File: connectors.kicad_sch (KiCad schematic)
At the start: 13 parts, among them J1 Conn_FFC_WE_68715014022, J2 Conn_FAKRA_2FAI-NZSP-PCBB6

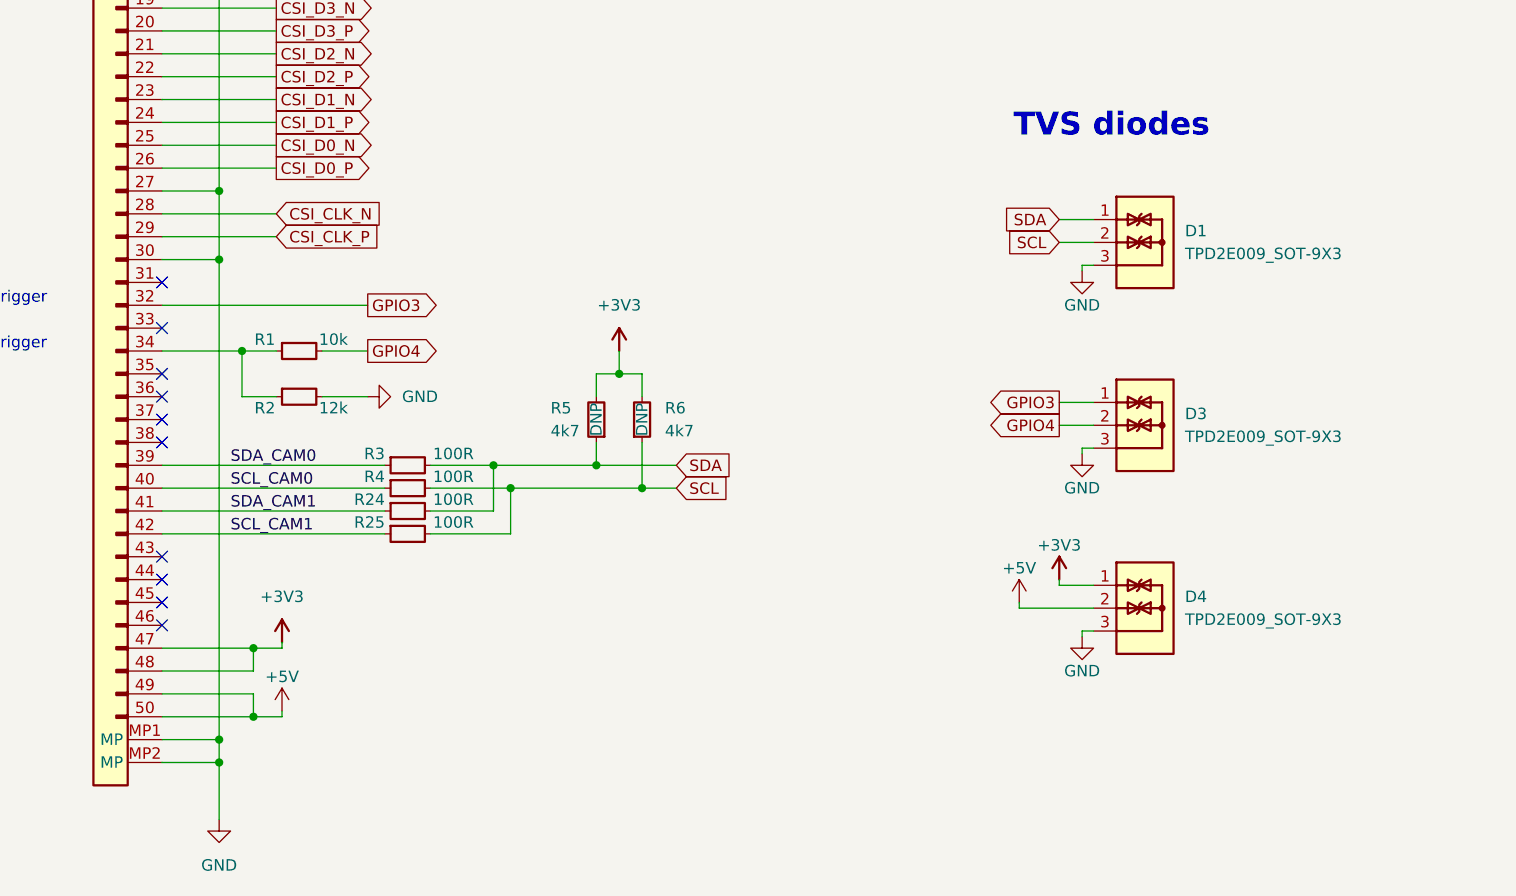
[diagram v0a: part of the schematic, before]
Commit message: Update TVS diodes
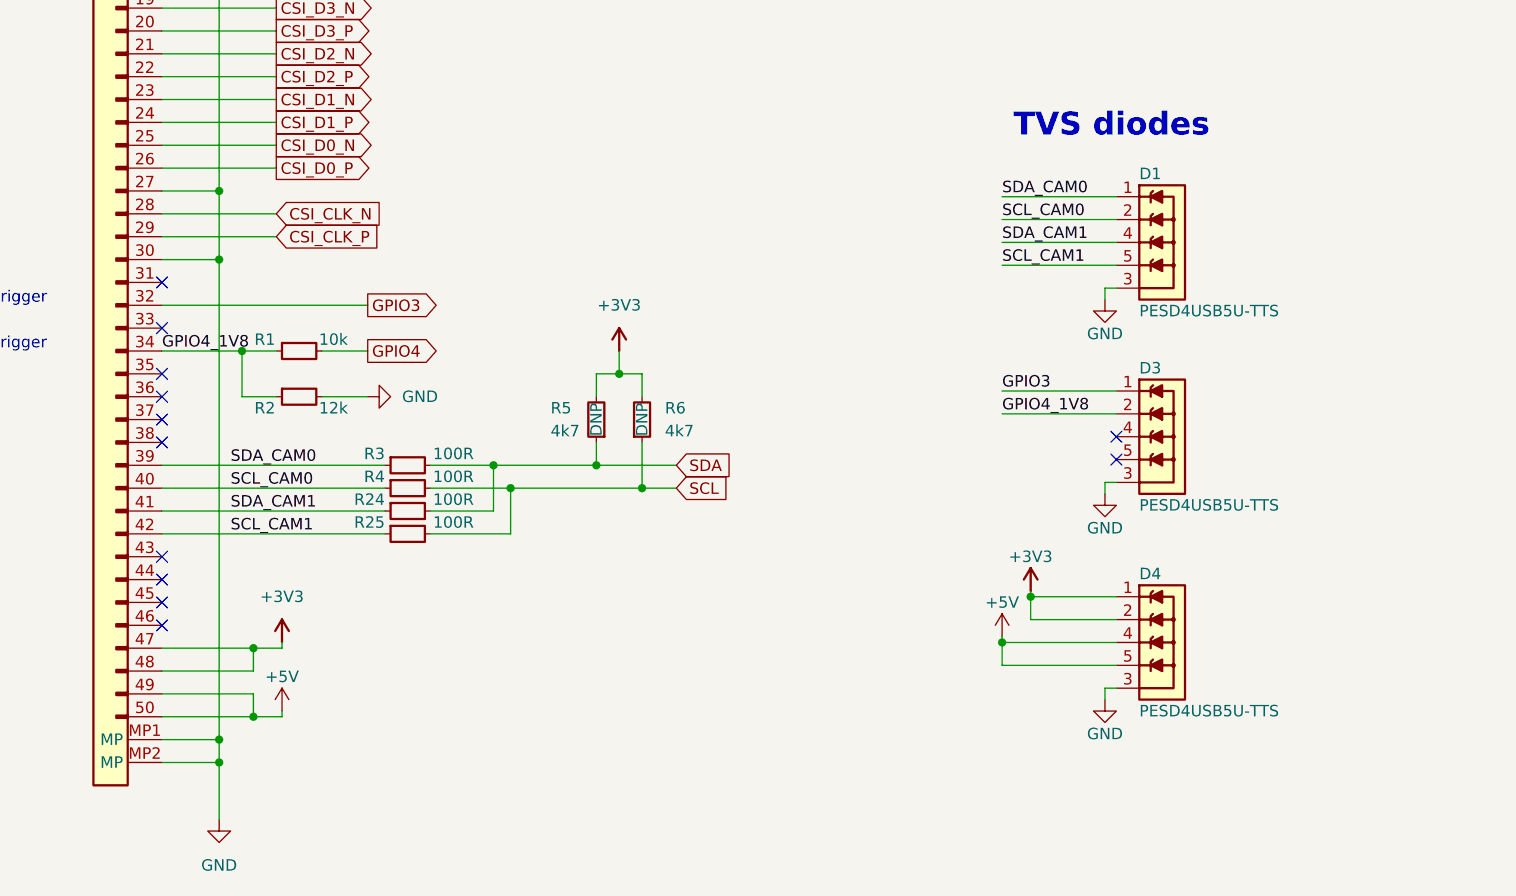
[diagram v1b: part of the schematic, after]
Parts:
- removed D1, D3, D4: TPD2E009_SOT-9X3, antmicro-footprints:SOT-723, symbol antmicroTVSDiodes:TPD2E009_SOT-9X3
- added D1, D3, D4: PESD4USB5U-TTS, antmicro-footprints:DFN-10_2.5x1mm, symbol antmicroTVSDiodes:PESD4USB5U-TTS
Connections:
- net +3V3: now also D4.1, D4.10, D4.2, D4.9
- net +5V: now also D4.4, D4.5, D4.6, D4.7
- net GND: now also D1.3, D1.8, D3.3, D3.8, D4.3, D4.8
- net GPIO3: now also D3.1, D3.10
- net SCL_CAM0: now also D1.2, D1.9
- net SCL_CAM1: now also D1.5, D1.6
- net SDA_CAM0: now also D1.1, D1.10
- net SDA_CAM1: now also D1.4, D1.7
- net GPIO4_1V8: now reaches J1.34, R1.1, R2.1
- net GPIO4_1V8: now also D3.2, D3.9
- new net: D3.4, D3.7
- new net: D3.5, D3.6
- no-connect marks 24 -> 26

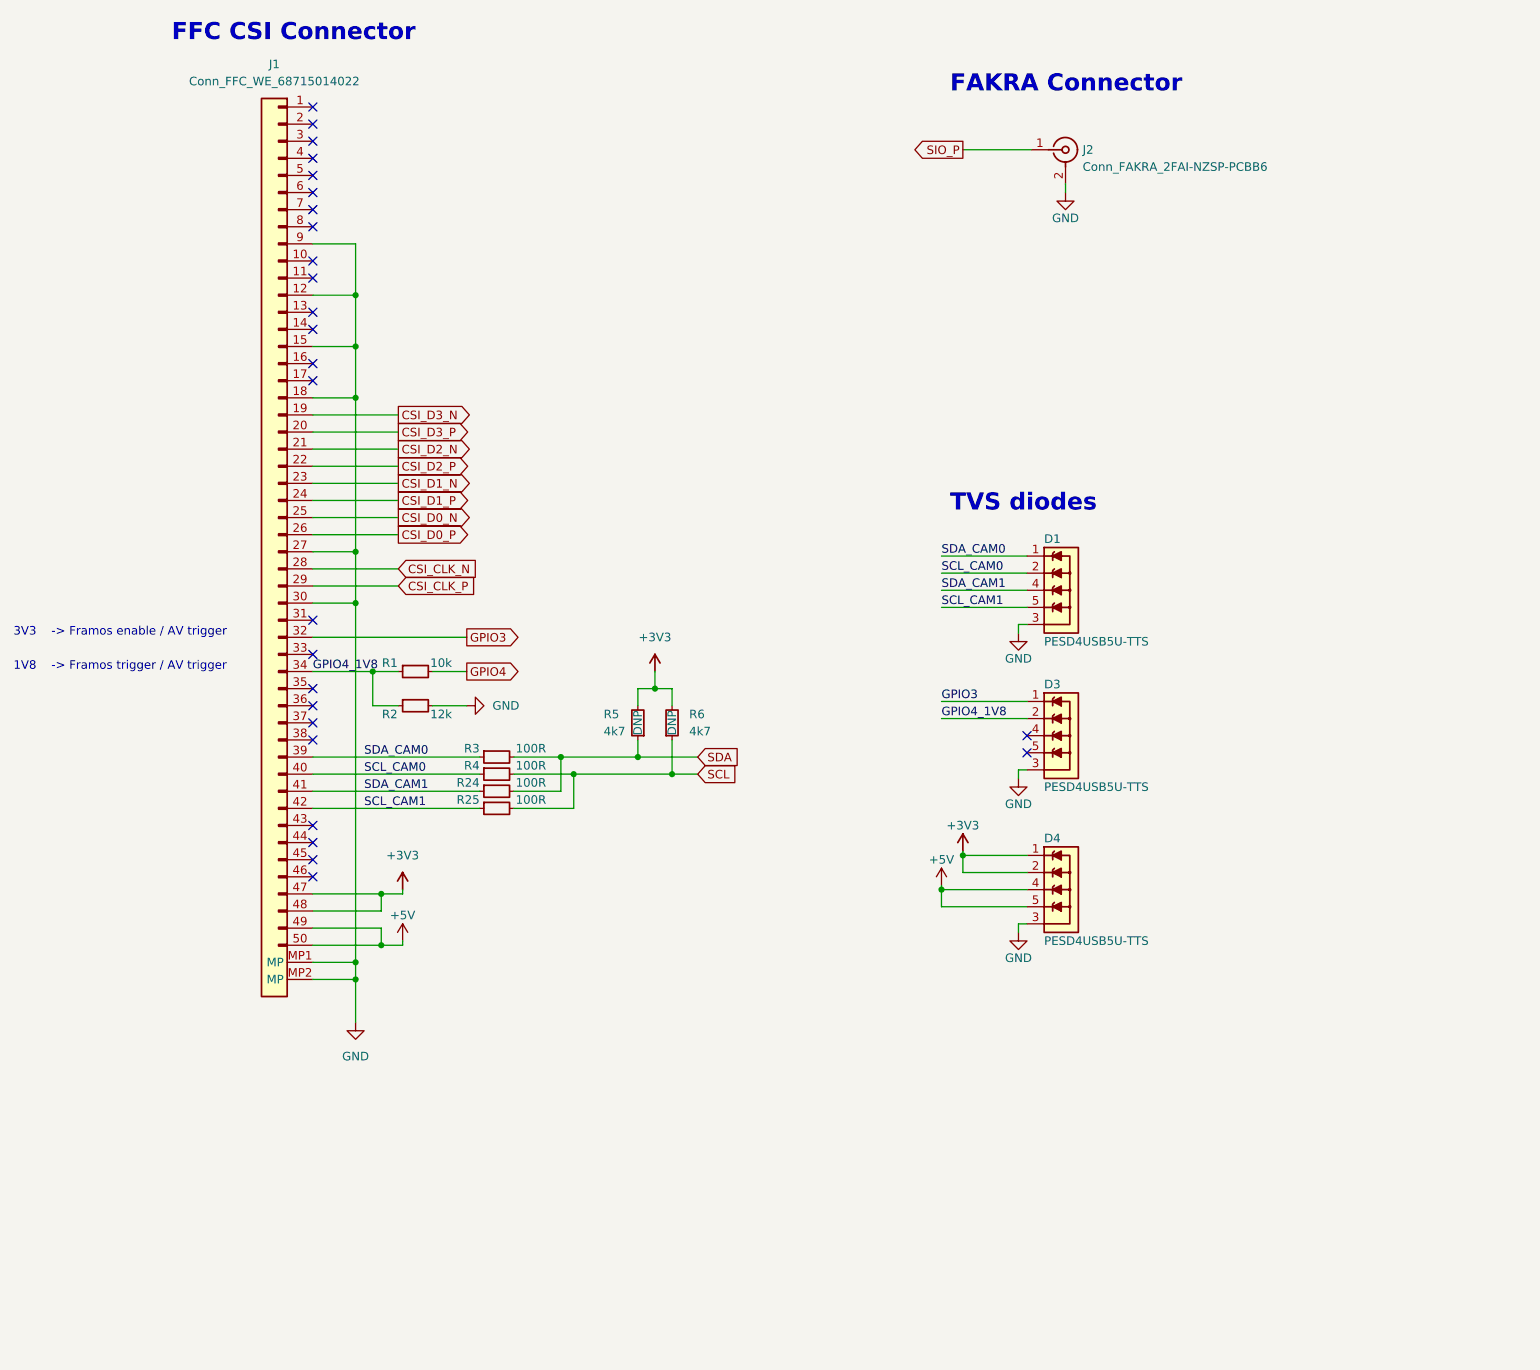
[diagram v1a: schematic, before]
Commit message: Update naming convention
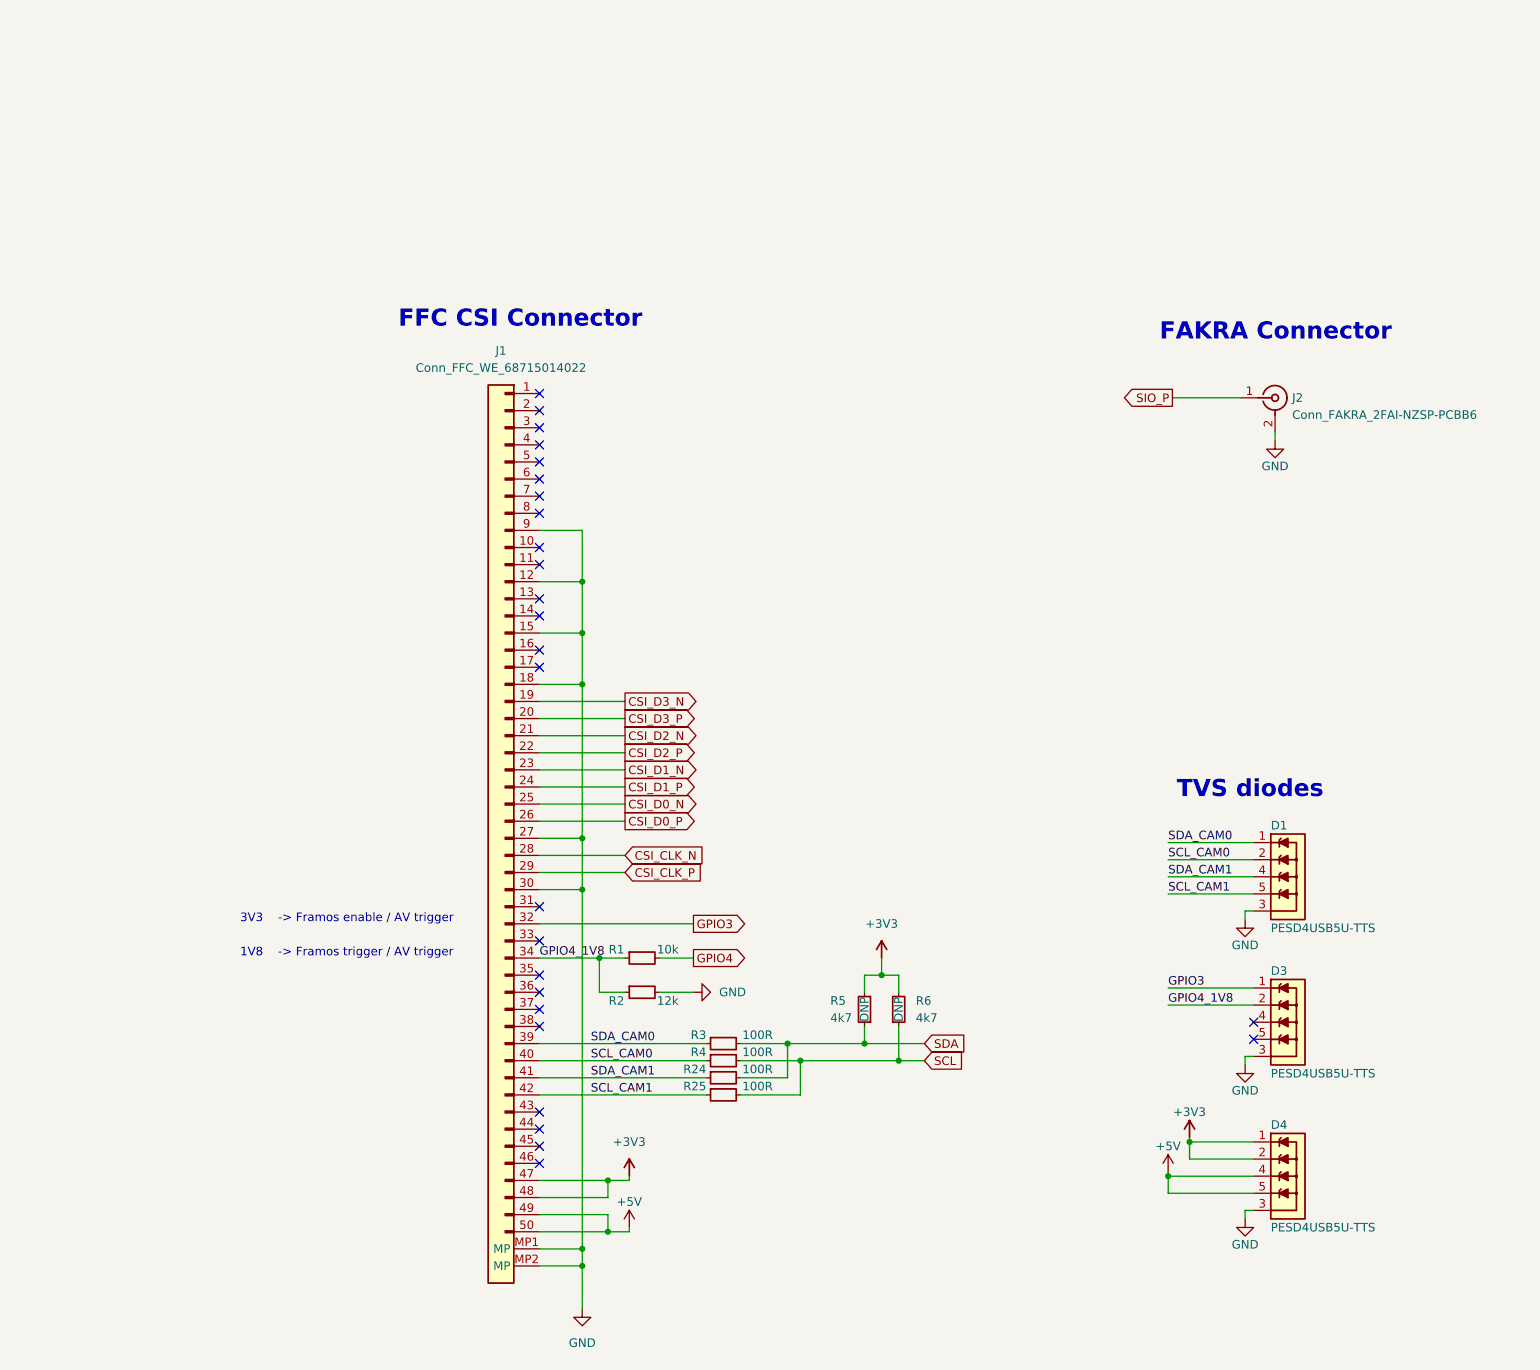
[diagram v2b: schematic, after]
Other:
- moved on the sheet: D1, D3, D4, J1, J2, R1, R2, R24, R25, R3, R4, R5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

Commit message: [#55438] Add LED indicators to schematics
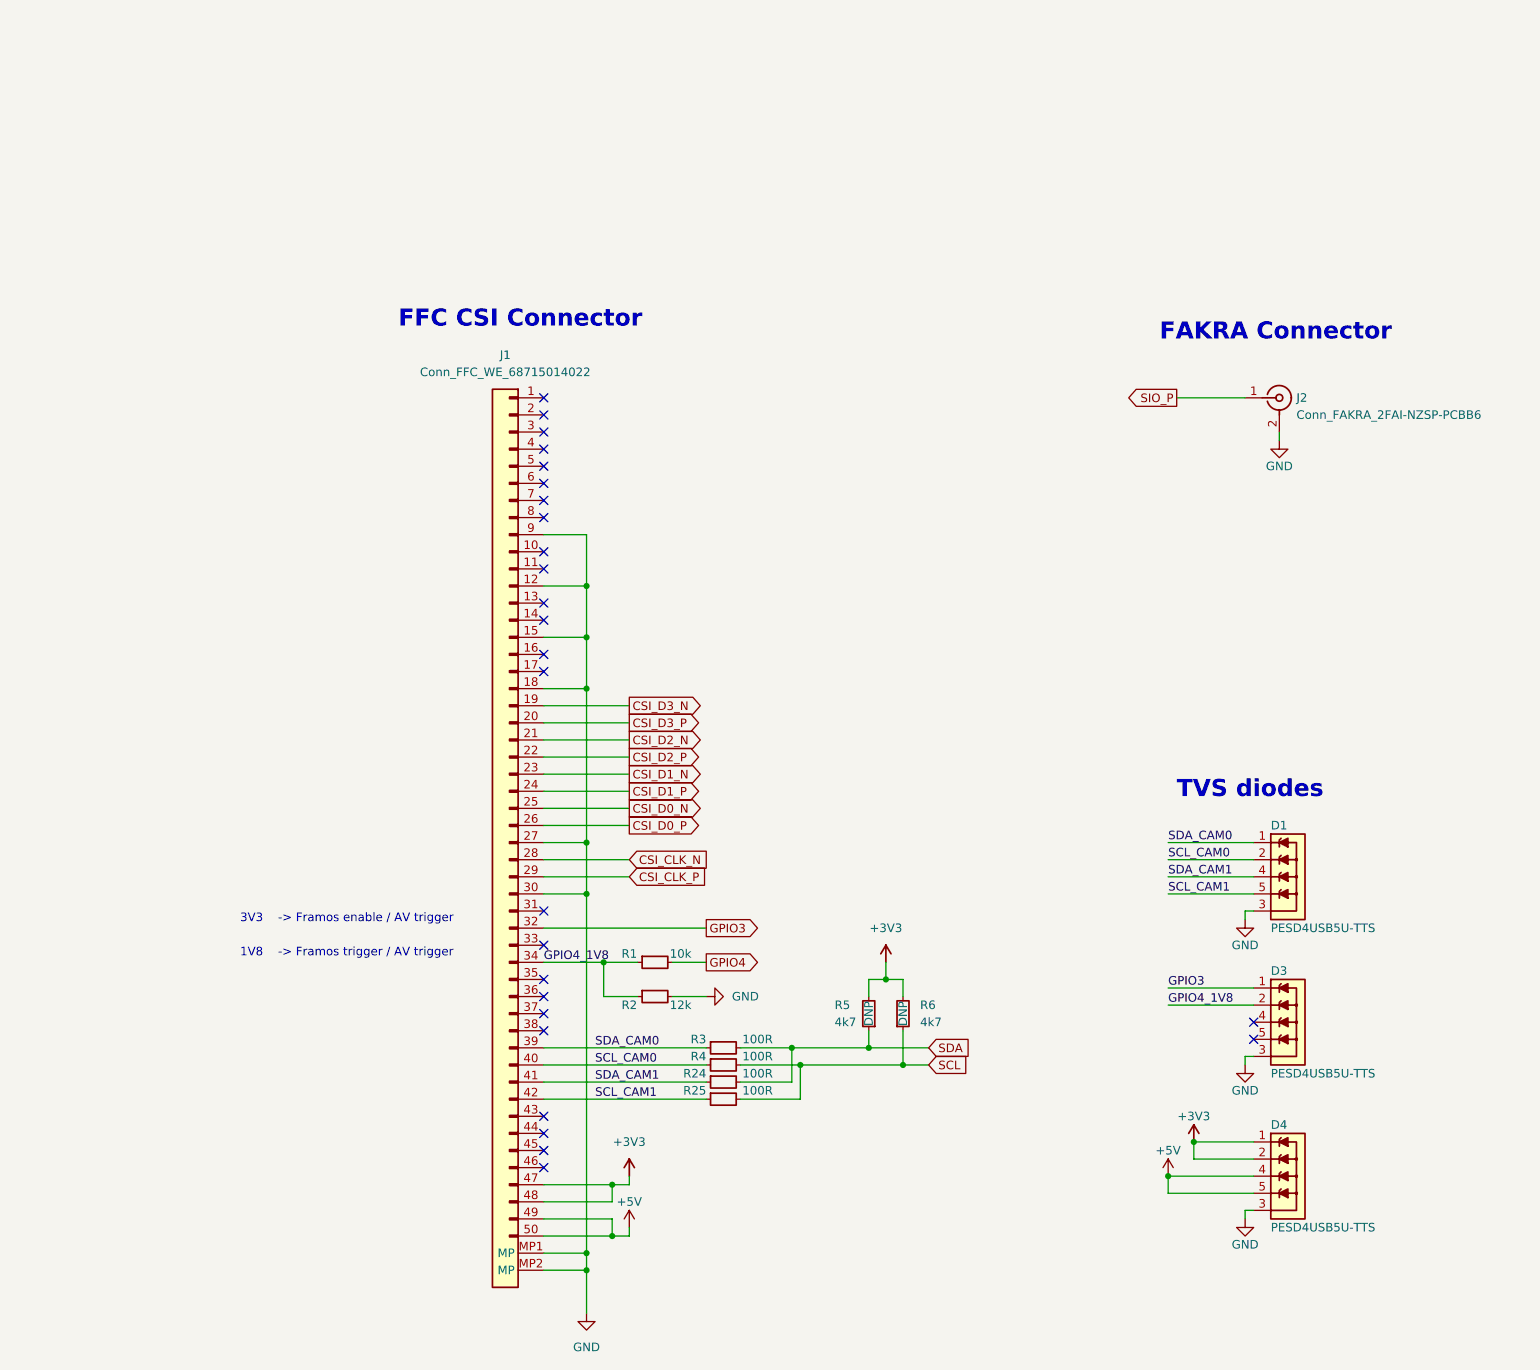
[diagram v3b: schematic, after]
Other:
- moved on the sheet: J1, J2, R1, R2, R24, R25, R3, R4, R5, R6

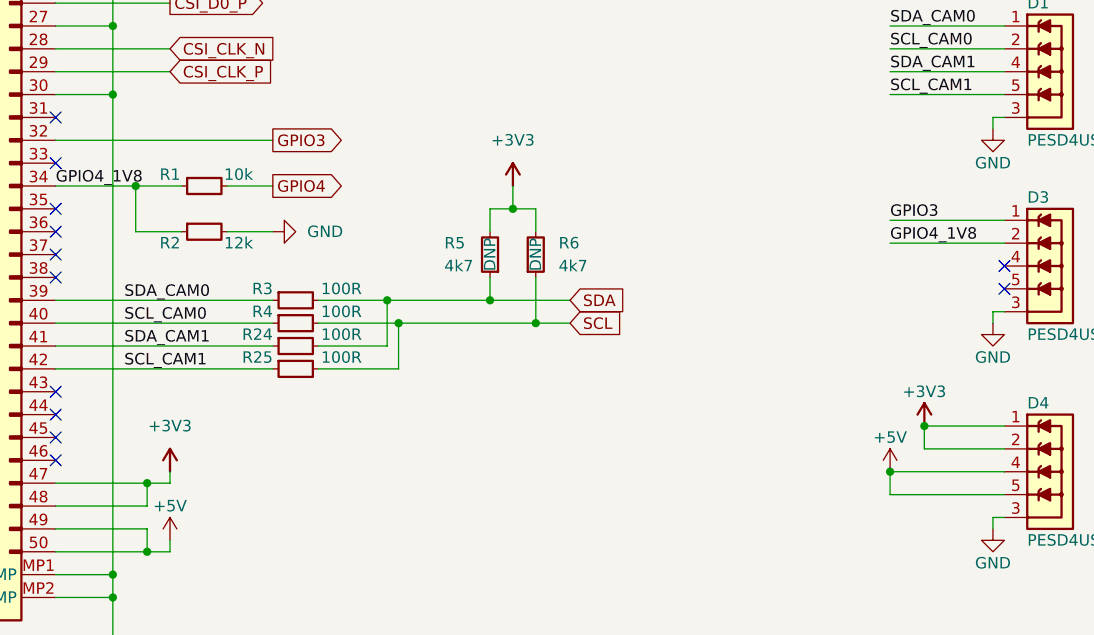
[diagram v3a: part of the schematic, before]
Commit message: [#55438] Place LED indicators on PCB
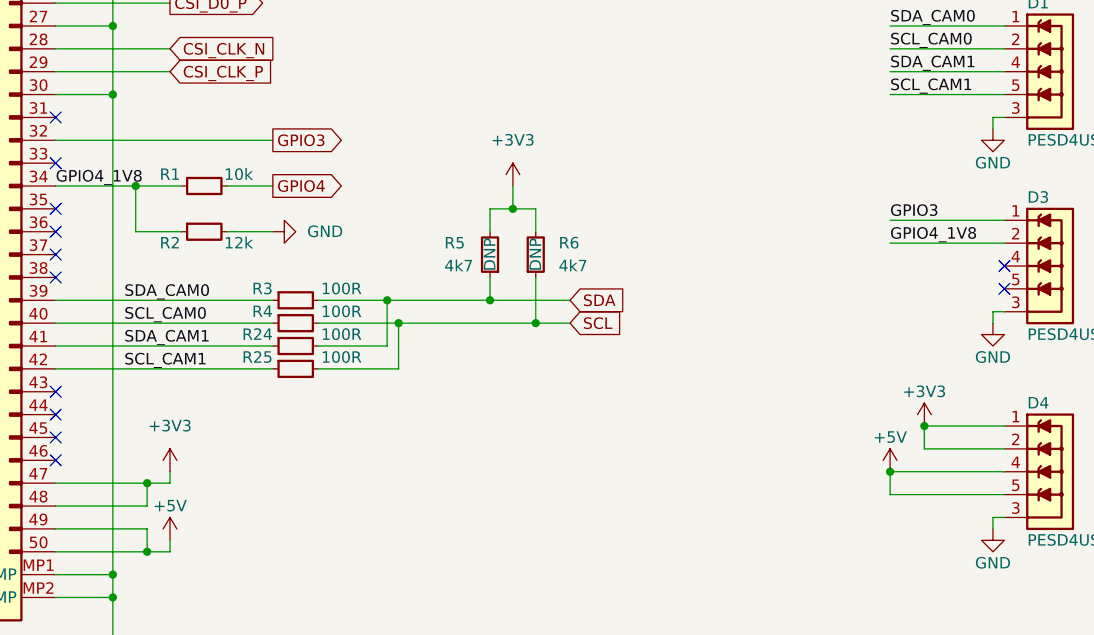
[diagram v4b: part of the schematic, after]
